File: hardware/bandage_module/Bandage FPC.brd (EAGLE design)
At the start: 14 parts

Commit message: Add remaining components and start board layout.
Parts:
- moved JP1 3.11 mm to (3.49, 8.49)
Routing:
- net AGND: track 92.1 -> 95.3 mm
- net SCL: track 89.4 -> 92.5 mm
- net N$5: track 12.3 -> 15.4 mm
- net N$3: track 30.1 -> 33.2 mm
- net +3V3: track 109.9 -> 113.0 mm
- net N$4: track 49.4 -> 52.5 mm
- net N$2: track 95.6 -> 98.7 mm
- net N$1: track 73.0 -> 76.1 mm
- net GND: track 159.0 -> 162.0 mm
- net SDA: track 89.1 -> 92.0 mm
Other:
- board text added: "BDG"
- board text added: "ECE492 G1"
- board text added: "R1"

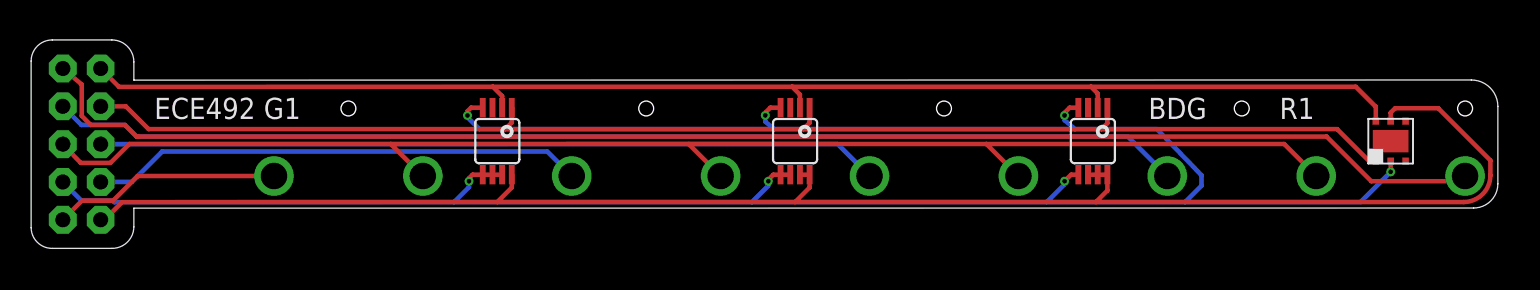
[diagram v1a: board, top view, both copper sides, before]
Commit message: Adding final draft of FPC
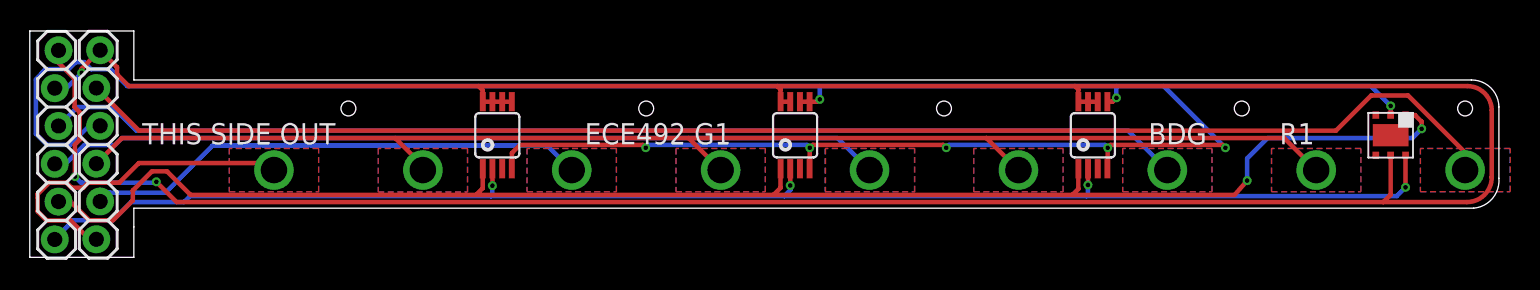
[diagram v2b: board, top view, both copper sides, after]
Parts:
- added JP2: (no value), SparkFun-Connectors:1X06_LOCK
- JP1: device SparkFun-Connectors:2X5_NOSILK -> SparkFun-Connectors:1X06_LOCK
- moved JP1 6.49 mm to (1.93, 14.8), turned to 270 degrees
- moved H1 0.40 mm to (96.4, 6.75)
- moved H2 0.40 mm to (76.4, 6.75)
- moved H3 0.40 mm to (56.4, 6.75)
- moved H4 0.40 mm to (36.4, 6.75)
- moved H5 0.40 mm to (16.4, 6.75)
- moved H6 0.40 mm to (26.4, 6.75)
- moved H7 0.40 mm to (46.4, 6.75)
- moved H8 0.40 mm to (66.4, 6.75)
- moved H9 0.40 mm to (86.4, 6.75)
- moved HUM 0.40 mm to (91.4, 9.09), turned to 180 degrees
- moved U$1 0.40 mm to (31.4, 9.09), turned to 0 degrees
- moved U$2 0.40 mm to (51.4, 9.09), turned to 0 degrees
- moved U$3 0.40 mm to (71.4, 9.09), turned to 0 degrees
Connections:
- net +3V3: now also JP1.1, JP1.2, JP2.6, U$1.5, U$1.6, U$1.7; no longer JP1.10
- net AGND: now also JP2.3; no longer JP1.5
- net GND: now also JP2.4; no longer JP1.7, U$1.5, U$1.6, U$1.7
- net N$2: now also JP2.5; no longer JP1.1
- net N$3: now also JP2.2; no longer JP1.8
- net N$4: now also JP1.4; no longer JP1.6
- net N$5: now also JP2.1; no longer JP1.9
- net SCL: now also JP1.6; no longer JP1.2
- net SDA: now also JP1.5; no longer JP1.4
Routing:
- net +3V3: track 113.0 -> 220.7 mm, vias 0 -> 3
- net SDA: track 92.0 -> 104.8 mm, vias 0 -> 2
- net N$5: track 15.4 -> 23.1 mm
- net SCL: track 92.5 -> 100.2 mm, vias 0 -> 4
- net N$4: track 52.5 -> 56.3 mm
- net AGND: track 95.3 -> 92.5 mm
- net GND: track 162.0 -> 164.6 mm, vias 7 -> 8
- net N$2: track 98.7 -> 96.9 mm
- net N$3: track 33.2 -> 33.9 mm
- net N$1: track 76.1 -> 76.7 mm
- added copper zone on layer 1, net AGND
- added copper zone on layer 16, net AGND
- added copper zone on layer 1, net N$1
- added copper zone on layer 16, net N$1
- added copper zone on layer 1, net N$2
- added copper zone on layer 16, net N$2
- added copper zone on layer 1, net N$3
- added copper zone on layer 16, net N$3
- added copper zone on layer 1, net N$4
- added copper zone on layer 16, net N$4
- added copper zone on layer 1, net N$5
- added copper zone on layer 16, net N$5
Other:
- board outline added: 98.7 x 15.2 mm
- board text added: "THIS SIDE OUT"
